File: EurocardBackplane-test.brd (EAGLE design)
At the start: 134.6 x 129.8 mm, 25 parts, among them IC1 LM399H, J1 JUMPER, U1 MIC5209, U2 WIZ820IO, U3 MIC5209-3.3YS, X5 FAC64S, X6 FAC64S, X7_AUX FAC64S

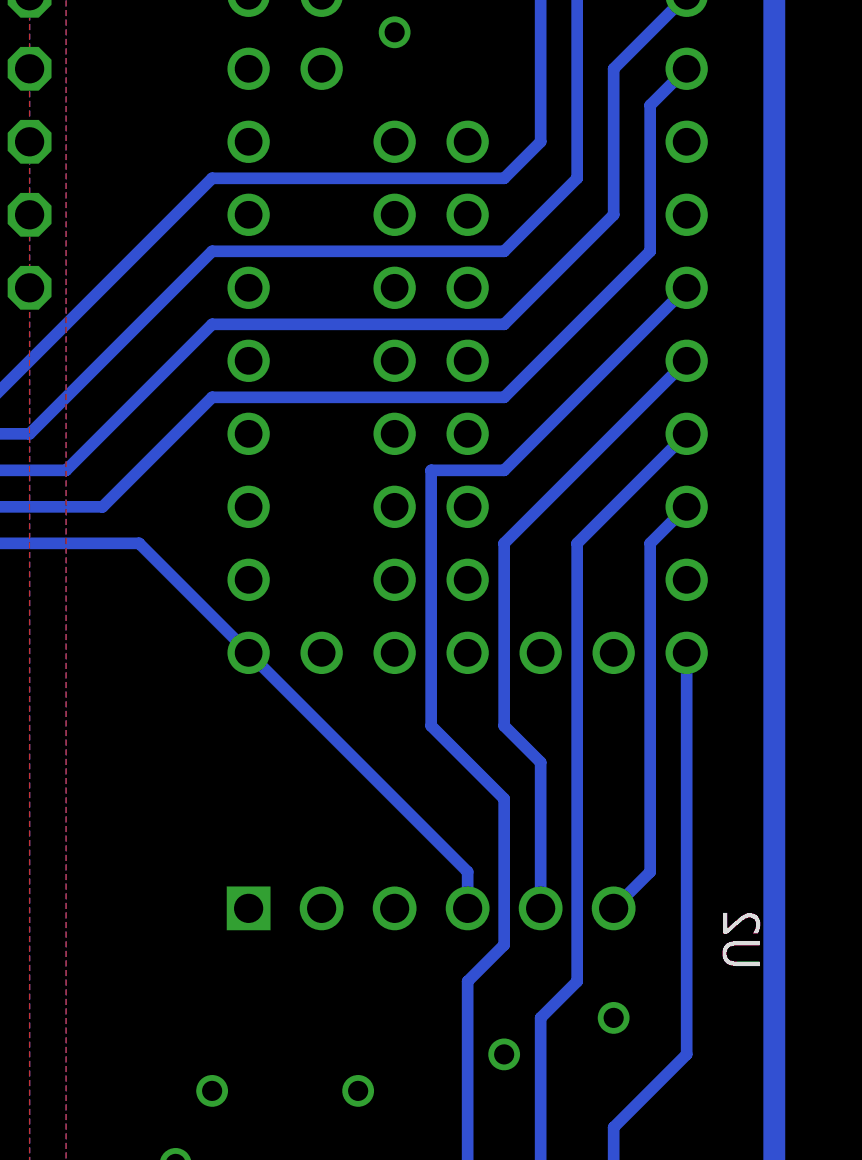
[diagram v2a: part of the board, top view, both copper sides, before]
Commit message: updated test backplane
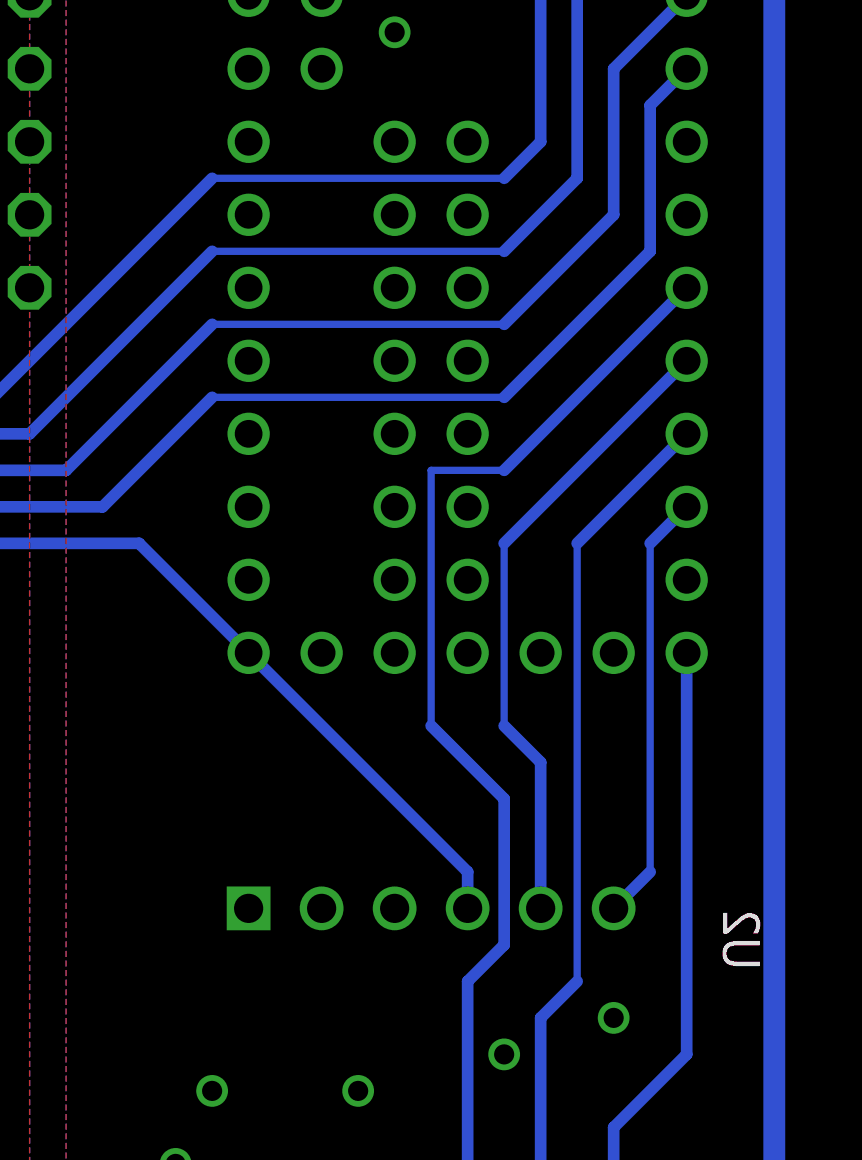
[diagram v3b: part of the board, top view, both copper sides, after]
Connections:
- removed net MOSI: U2.MOSI
- net SPI_MOSI: now also U2.MOSI
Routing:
- net SPI_MOSI: track 104.2 -> 121.4 mm
- net SPI_C0: track 53.8 -> 52.3 mm
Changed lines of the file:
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@@
 <?xml version="1.0" encoding="utf-8"?>
 <!DOCTYPE eagle SYSTEM "eagle.dtd">
-<eagle version="6.5.0">
+<eagle version="6.6.0">
 <drawing>
 <settings>
@@
 <via x="11.43" y="43.18" extent="1-16" drill="0.7"/>
 </signal>
-<signal name="MOSI">
-<contactref element="U2" pad="MOSI"/>
-</signal>
 <signal name="SPI_MISO">
 <contactref element="U2" pad="MISO"/>
@@
 <contactref element="TEENSY" pad="8"/>
 <wire x1="119.38" y1="76.2" x2="125.73" y2="82.55" width="0.4064" layer="16"/>
-<wire x1="119.38" y1="76.2" x2="119.38" y2="69.85" width="0.4064" layer="16"/>
+<wire x1="119.38" y1="76.2" x2="119.38" y2="69.85" width="0.254" layer="16"/>
 <wire x1="119.38" y1="69.85" x2="120.65" y2="68.58" width="0.4064" layer="16"/>
 <wire x1="120.65" y1="68.58" x2="120.65" y2="63.5" width="0.4064" layer="16"/>
@@
 <wire x1="119.38" y1="62.23" x2="119.38" y2="67.31" width="0.4064" layer="16"/>
 <wire x1="119.38" y1="67.31" x2="116.84" y2="69.85" width="0.4064" layer="16"/>
-<wire x1="116.84" y1="69.85" x2="116.84" y2="78.74" width="0.4064" layer="16"/>
-<wire x1="116.84" y1="78.74" x2="119.38" y2="78.74" width="0.4064" layer="16"/>
+<wire x1="116.84" y1="69.85" x2="116.84" y2="78.74" width="0.254" layer="16"/>
+<wire x1="116.84" y1="78.74" x2="119.38" y2="78.74" width="0.254" layer="16"/>
 </signal>
 <signal name="WIZNET_RESET">
@@
 <wire x1="120.65" y1="59.69" x2="121.92" y2="60.96" width="0.4064" layer="16"/>
 <contactref element="TEENSY" pad="9"/>
-<wire x1="121.92" y1="60.96" x2="121.92" y2="76.2" width="0.4064" layer="16"/>
+<wire x1="121.92" y1="60.96" x2="121.92" y2="76.2" width="0.254" layer="16"/>
 <wire x1="121.92" y1="76.2" x2="125.73" y2="80.01" width="0.4064" layer="16"/>
 </signal>
@@
 <contactref element="TEENSY" pad="10"/>
 <wire x1="125.73" y1="77.47" x2="124.46" y2="76.2" width="0.4064" layer="16"/>
-<wire x1="124.46" y1="76.2" x2="124.46" y2="64.77" width="0.4064" layer="16"/>
+<wire x1="124.46" y1="76.2" x2="124.46" y2="64.77" width="0.254" layer="16"/>
 <wire x1="124.46" y1="64.77" x2="123.19" y2="63.5" width="0.4064" layer="16"/>
 </signal>
@@
 <wire x1="105.41" y1="74.93" x2="109.22" y2="71.12" width="0.4064" layer="2"/>
 <wire x1="109.22" y1="71.12" x2="121.92" y2="71.12" width="0.4064" layer="2"/>
-<wire x1="121.92" y1="71.12" x2="121.92" y2="73.66" width="0.4064" layer="2"/>
+<wire x1="121.92" y1="71.12" x2="121.92" y2="73.66" width="0.254" layer="2"/>
 <wire x1="121.92" y1="73.66" x2="123.19" y2="74.93" width="0.4064" layer="2"/>
 <wire x1="123.19" y1="74.93" x2="125.73" y2="74.93" width="0.4064" layer="2"/>
@@
 <wire x1="62.23" y1="73.66" x2="60.96" y2="74.93" width="0.4064" layer="16"/>
 <wire x1="60.96" y1="74.93" x2="31.75" y2="74.93" width="0.4064" layer="16"/>
+<contactref element="U2" pad="MOSI"/>
+<wire x1="115.57" y1="63.5" x2="121.92" y2="69.85" width="0.4064" layer="15"/>
+<wire x1="121.92" y1="69.85" x2="121.92" y2="73.66" width="0.254" layer="15"/>
+<wire x1="121.92" y1="73.66" x2="123.19" y2="74.93" width="0.4064" layer="15"/>
+<wire x1="123.19" y1="74.93" x2="125.73" y2="74.93" width="0.4064" layer="15"/>
 </signal>
 <signal name="GPIO#0">
@@
 <contactref element="JP2" pad="1"/>
 <wire x1="102.87" y1="102.87" x2="109.22" y2="96.52" width="0.4064" layer="2"/>
-<wire x1="109.22" y1="96.52" x2="111.76" y2="96.52" width="0.4064" layer="2"/>
-<wire x1="111.76" y1="96.52" x2="111.76" y2="73.66" width="0.4064" layer="2"/>
-<wire x1="111.76" y1="73.66" x2="113.03" y2="72.39" width="0.4064" layer="2"/>
+<wire x1="109.22" y1="96.52" x2="111.76" y2="96.52" width="0.254" layer="2"/>
+<wire x1="113.03" y1="72.39" x2="113.03" y2="90.17" width="0.4064" layer="2"/>
+<wire x1="113.03" y1="90.17" x2="111.76" y2="91.44" width="0.4064" layer="2"/>
+<wire x1="111.76" y1="91.44" x2="111.76" y2="96.52" width="0.254" layer="2"/>
 </signal>
 <signal name="GPIO#1">
@@
 <wire x1="96.52" y1="81.28" x2="101.6" y2="81.28" width="0.4064" layer="16"/>
 <wire x1="101.6" y1="81.28" x2="109.22" y2="88.9" width="0.4064" layer="16"/>
-<wire x1="109.22" y1="88.9" x2="119.38" y2="88.9" width="0.4064" layer="16"/>
+<wire x1="109.22" y1="88.9" x2="119.38" y2="88.9" width="0.254" layer="16"/>
 <wire x1="119.38" y1="88.9" x2="120.65" y2="90.17" width="0.4064" layer="16"/>
 <wire x1="63.627" y1="81.28" x2="63.5" y2="81.407" width="0.4064" layer="16"/>
@@
 <wire x1="96.52" y1="80.01" x2="102.87" y2="80.01" width="0.4064" layer="16"/>
 <wire x1="102.87" y1="80.01" x2="109.22" y2="86.36" width="0.4064" layer="16"/>
-<wire x1="109.22" y1="86.36" x2="119.38" y2="86.36" width="0.4064" layer="16"/>
+<wire x1="109.22" y1="86.36" x2="119.38" y2="86.36" width="0.254" layer="16"/>
 <wire x1="119.38" y1="86.36" x2="121.92" y2="88.9" width="0.4064" layer="16"/>
 <wire x1="62.23" y1="80.01" x2="60.96" y2="81.28" width="0.4064" layer="16"/>
@@
 <wire x1="96.52" y1="78.74" x2="104.14" y2="78.74" width="0.4064" layer="16"/>
 <wire x1="104.14" y1="78.74" x2="109.22" y2="83.82" width="0.4064" layer="16"/>
-<wire x1="109.22" y1="83.82" x2="119.38" y2="83.82" width="0.4064" layer="16"/>
+<wire x1="109.22" y1="83.82" x2="119.38" y2="83.82" width="0.254" layer="16"/>
 <wire x1="119.38" y1="83.82" x2="123.19" y2="87.63" width="0.4064" layer="16"/>
 <wire x1="63.627" y1="78.74" x2="63.5" y2="78.867" width="0.4064" layer="16"/>
@@
 <wire x1="96.52" y1="77.47" x2="105.41" y2="77.47" width="0.4064" layer="16"/>
 <wire x1="105.41" y1="77.47" x2="109.22" y2="81.28" width="0.4064" layer="16"/>
-<wire x1="109.22" y1="81.28" x2="119.38" y2="81.28" width="0.4064" layer="16"/>
+<wire x1="109.22" y1="81.28" x2="119.38" y2="81.28" width="0.254" layer="16"/>
 <wire x1="119.38" y1="81.28" x2="124.46" y2="86.36" width="0.4064" layer="16"/>
 <wire x1="124.46" y1="86.36" x2="124.46" y2="91.44" width="0.4064" layer="16"/>
@@
 <contactref element="TEENSY" pad="33"/>
 <wire x1="115.57" y1="85.09" x2="111.76" y2="88.9" width="0.4064" layer="15"/>
-<wire x1="111.76" y1="88.9" x2="106.68" y2="88.9" width="0.4064" layer="15"/>
+<wire x1="111.76" y1="88.9" x2="106.68" y2="88.9" width="0.254" layer="15"/>
 <wire x1="106.68" y1="88.9" x2="104.14" y2="86.36" width="0.4064" layer="15"/>
 <wire x1="104.14" y1="86.36" x2="99.06" y2="86.36" width="0.4064" layer="15"/>
@@
 <wire x1="116.84" y1="83.82" x2="114.3" y2="83.82" width="0.4064" layer="15"/>
 <wire x1="114.3" y1="83.82" x2="111.76" y2="81.28" width="0.4064" layer="15"/>
-<wire x1="111.76" y1="81.28" x2="107.95" y2="81.28" width="0.4064" layer="15"/>
+<wire x1="111.76" y1="81.28" x2="107.95" y2="81.28" width="0.254" layer="15"/>
 <wire x1="95.25" y1="64.77" x2="87.63" y2="64.77" width="0.4064" layer="15"/>
 <wire x1="87.63" y1="64.77" x2="86.36" y2="66.04" width="0.4064" layer="15"/>
@@
 <contactref element="TEENSY" pad="32"/>
 <wire x1="115.57" y1="82.55" x2="111.76" y2="78.74" width="0.4064" layer="15"/>
-<wire x1="111.76" y1="78.74" x2="107.95" y2="78.74" width="0.4064" layer="15"/>
+<wire x1="111.76" y1="78.74" x2="107.95" y2="78.74" width="0.254" layer="15"/>
 <wire x1="107.95" y1="78.74" x2="104.14" y2="74.93" width="0.4064" layer="15"/>
 <wire x1="104.14" y1="74.93" x2="104.14" y2="71.12" width="0.4064" layer="15"/>
@@
 <contactref element="TEENSY" pad="31"/>
 <wire x1="115.57" y1="80.01" x2="111.76" y2="76.2" width="0.4064" layer="15"/>
-<wire x1="111.76" y1="76.2" x2="107.95" y2="76.2" width="0.4064" layer="15"/>
+<wire x1="111.76" y1="76.2" x2="107.95" y2="76.2" width="0.254" layer="15"/>
 <wire x1="107.95" y1="76.2" x2="105.41" y2="73.66" width="0.4064" layer="15"/>
 <wire x1="105.41" y1="73.66" x2="105.41" y2="69.85" width="0.4064" layer="15"/>
@@
 <wire x1="109.22" y1="68.58" x2="111.76" y2="68.58" width="0.4064" layer="15"/>
 <wire x1="111.76" y1="68.58" x2="114.3" y2="71.12" width="0.4064" layer="15"/>
-<wire x1="114.3" y1="71.12" x2="114.3" y2="73.66" width="0.4064" layer="15"/>
+<wire x1="114.3" y1="71.12" x2="114.3" y2="73.66" width="0.254" layer="15"/>
 <wire x1="114.3" y1="73.66" x2="115.57" y2="74.93" width="0.4064" layer="15"/>
 </signal>
@@
 <wire x1="95.25" y1="49.53" x2="85.09" y2="49.53" width="0.4064" layer="15"/>
 <wire x1="95.25" y1="49.53" x2="106.68" y2="60.96" width="0.4064" layer="15"/>
-<wire x1="106.68" y1="60.96" x2="115.57" y2="60.96" width="0.4064" layer="15"/>
-<wire x1="115.57" y1="60.96" x2="116.84" y2="62.23" width="0.4064" layer="15"/>
-<wire x1="116.84" y1="62.23" x2="116.84" y2="67.31" width="0.4064" layer="15"/>
-<wire x1="116.84" y1="67.31" x2="119.38" y2="69.85" width="0.4064" layer="15"/>
-<wire x1="119.38" y1="69.85" x2="119.38" y2="76.2" width="0.4064" layer="15"/>
+<wire x1="119.38" y1="69.85" x2="119.38" y2="76.2" width="0.254" layer="15"/>
 <wire x1="119.38" y1="76.2" x2="118.11" y2="77.47" width="0.4064" layer="15"/>
+<wire x1="106.68" y1="60.96" x2="113.03" y2="60.96" width="0.4064" layer="15"/>
+<wire x1="113.03" y1="60.96" x2="114.3" y2="62.23" width="0.4064" layer="15"/>
+<wire x1="114.3" y1="62.23" x2="114.3" y2="64.77" width="0.254" layer="15"/>
+<wire x1="114.3" y1="64.77" x2="119.38" y2="69.85" width="0.4064" layer="15"/>
 </signal>
 <signal name="SPI_CS3">
 <contactref element="TEENSY" pad="30"/>
 <wire x1="115.57" y1="77.47" x2="111.76" y2="73.66" width="0.4064" layer="15"/>
-<wire x1="111.76" y1="73.66" x2="109.22" y2="73.66" width="0.4064" layer="15"/>
+<wire x1="111.76" y1="73.66" x2="109.22" y2="73.66" width="0.254" layer="15"/>
 <wire x1="109.22" y1="73.66" x2="106.68" y2="71.12" width="0.4064" layer="15"/>
 <wire x1="106.68" y1="71.12" x2="106.68" y2="68.58" width="0.4064" layer="15"/>
